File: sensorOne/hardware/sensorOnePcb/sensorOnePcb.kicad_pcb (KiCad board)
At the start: 4 copper layers, 71.4 x 38 mm, 74 parts, among them J1 Conn_01x04_Pin, J2 Screw_Terminal_01x08, J3 Conn_ARM_SWD_TagConnect_TC2030, J4 Conn_01x03_Pin, U1 MSPM0G3507SPTR, U2 MCP2562-H-SN, U3 MAX31856, U4 MAX31856, U5 SPX3819M5-L-5-0, U6 SPX3819M5-L-3-3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

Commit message: PCB cleanup
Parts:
- added G***: LOGO, cavemanSensors:wcoffroadsmall, F.Cu at (123.9, 95.5)
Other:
- board text added: "${boardNameShort}"
- board text added: "Rev: ${VERSION}"
- board text removed: "${boardName} Rev ${Revision}"

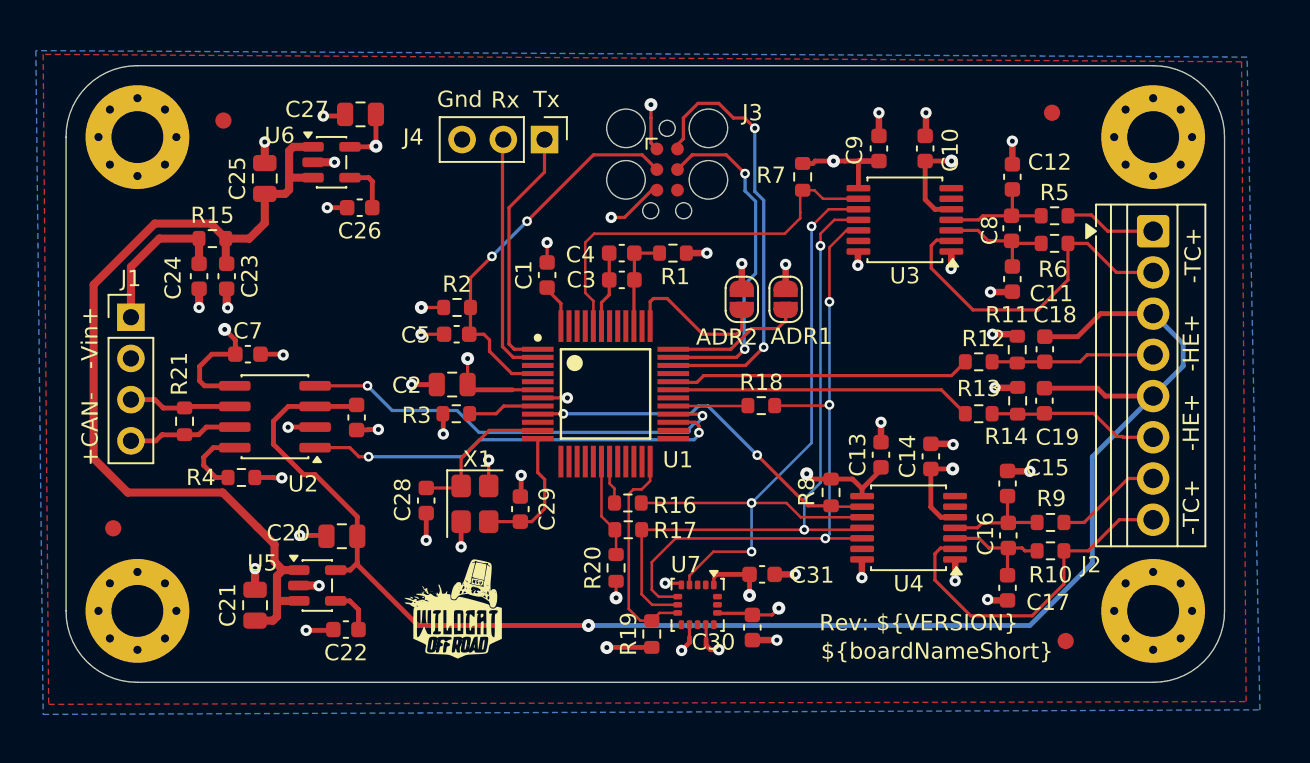
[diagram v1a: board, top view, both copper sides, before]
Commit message: main connector now 2mm jst, added package details
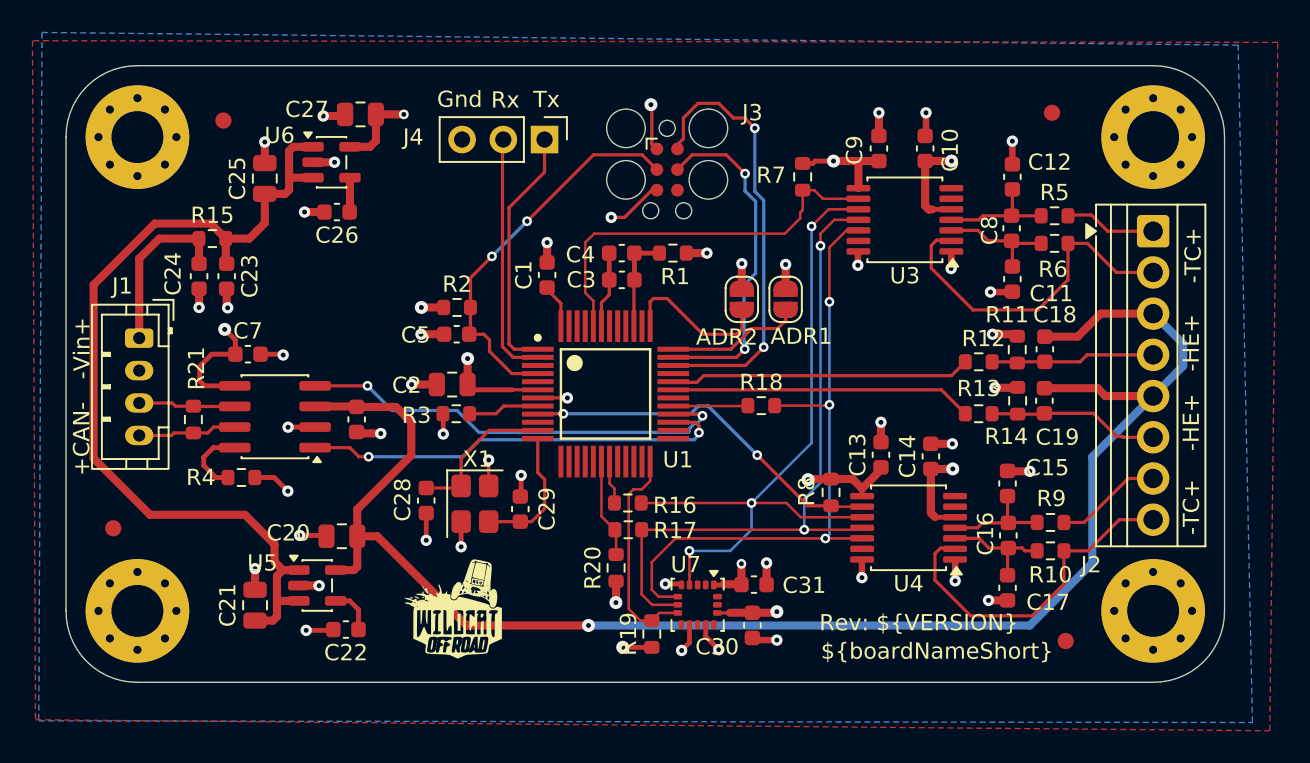
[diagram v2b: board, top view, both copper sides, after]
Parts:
- J1: footprint Connector_PinHeader_2.54mm:PinHeader_1x04_P2.54mm_Vertical -> Connector_JST:JST_PH_B4B-PH-K_1x04_P2.00mm_Vertical
- U3, U4: value MAX31856 -> MAX31856MUD+
- moved C26 1.43 mm to (116.7, 71.0)
- moved J1 1.39 mm to (104.5, 78.8), turned to -90 degrees
- moved C31 0.80 mm to (142.4, 94.0)
- moved R21 0.56 mm to (107.8, 83.8)
- moved C30 0.14 mm to (142.3, 96.5)
- moved C6 0.12 mm to (117.9, 83.8)
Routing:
- net VCC: track 9.57 -> 10.6 mm
- net /BYP_3V3: track 3.09 -> 2.13 mm
- net GND: track 65.6 -> 66.3 mm
- net /CAN+: track 6.68 -> 6.11 mm
- net /CAN-: track 6.61 -> 6.10 mm
- net +5V: track 99.7 -> 100.2 mm

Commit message: pcb clean up
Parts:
- added G***: LOGO, cavemanSensors:cavemanSensorsSmall, F.Cu at (116.8, 77.2)
- moved G*** 1.72 mm to (125.6, 95.5)
- moved C21 0.64 mm to (111.6, 94.6)
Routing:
- net GND: track 66.3 -> 71.0 mm, vias 46 -> 98
- net VCCF: track 56.0 -> 60.4 mm
- net /CAN_RX: track 27.6 -> 23.8 mm
- net /CAN_TX: track 26.7 -> 23.2 mm
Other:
- board text added: "NOT FOR FLIGHT"
